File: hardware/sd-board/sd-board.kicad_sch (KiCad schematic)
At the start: 9 parts, among them J1 TF-01A push-push, J2 FFC 6P 0.5mm, U1 74LVC1G04

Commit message: feat(hardware): SD board v4, the user's plan: a 28.8 x 44.5 mm board right of the battery by its plug (the battery stays), the card through the bottom wall flush with the outside at 86 mm from the left wall, the cover's pole in a half-round seat, the FFC from the jacks' gap down to the top; FFC order 3V3 CS MOSI GND CLK MISO (the card's contacts' order, nothing crosses); all sizes measured (MEASUREMENTS.md); DRC 0, nets 0 differ
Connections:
- net 3V3: now also J2.1 (Pin_1); no longer J2.5 (Pin_5)
- net CLK: now also J2.5 (Pin_5); no longer J2.2 (Pin_2)
- net LCD_CS: now also J2.2 (Pin_2); no longer J2.6 (Pin_6)
- net MISO: now also J2.6 (Pin_6); no longer J2.3 (Pin_3)
- net MOSI: now also J2.3 (Pin_3); no longer J2.1 (Pin_1)
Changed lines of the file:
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@@
 (label "3V3" (at 76.2 128.27 270) (effects (font (size 1.27 1.27)) (justify left bottom)))
 (symbol (lib_id "Connector_Generic_MountingPin:Conn_01x06_MountingPin") (at 231.14 88.9 0) (unit 1) (exclude_from_sim no) (in_bom yes) (on_board yes) (dnp no) (property "Reference" "J2" (at 231.14 74.9 0) (effects (font (size 1.27 1.27)))) (property "Value" "FFC 6P 0.5mm" (at 231.14 102.9 0) (effects (font (size 1.27 1.27)))) (property "Footprint" "sdboard:FPC-SMD_6P-P0.50_XUNPU_FPC-05F-6PH20" (at 231.14 88.9 0) (effects (font (size 1.27 1.27)) (hide yes))) (property "Datasheet" "" (at 231.14 88.9 0) (effects (font (size 1.27 1.27)) (hide yes))) (property "LCSC" "C2856796" (at 231.14 88.9 0) (effects (font (size 1.27 1.27)) (hide yes))) (pin "1") (pin "2") (pin "3") (pin "4") (pin "5") (pin "6") (pin "MP") (instances (project "sd-board" (path "/766c70bd-1acb-59f5-b703-96c0315a8041" (reference "J2") (unit 1)))))
-(label "MOSI" (at 226.06 83.82 180) (effects (font (size 1.27 1.27)) (justify right bottom)))
-(label "CLK" (at 226.06 86.36 180) (effects (font (size 1.27 1.27)) (justify right bottom)))
-(label "MISO" (at 226.06 88.9 180) (effects (font (size 1.27 1.27)) (justify right bottom)))
+(label "3V3" (at 226.06 83.82 180) (effects (font (size 1.27 1.27)) (justify right bottom)))
+(label "LCD_CS" (at 226.06 86.36 180) (effects (font (size 1.27 1.27)) (justify right bottom)))
+(label "MOSI" (at 226.06 88.9 180) (effects (font (size 1.27 1.27)) (justify right bottom)))
 (label "GND" (at 226.06 91.44 180) (effects (font (size 1.27 1.27)) (justify right bottom)))
-(label "3V3" (at 226.06 93.98 180) (effects (font (size 1.27 1.27)) (justify right bottom)))
-(label "LCD_CS" (at 226.06 96.52 180) (effects (font (size 1.27 1.27)) (justify right bottom)))
+(label "CLK" (at 226.06 93.98 180) (effects (font (size 1.27 1.27)) (justify right bottom)))
+(label "MISO" (at 226.06 96.52 180) (effects (font (size 1.27 1.27)) (justify right bottom)))
 (label "GND" (at 231.14 101.6 270) (effects (font (size 1.27 1.27)) (justify left bottom)))
 (symbol (lib_id "power:PWR_FLAG") (at 40.64 149.86 0) (unit 1) (exclude_from_sim no) (in_bom no) (on_board no) (dnp no) (property "Reference" "#FLG01" (at 40.64 135.86 0) (effects (font (size 1.27 1.27)) (hide yes))) (property "Value" "PWR_FLAG" (at 40.64 163.86 0) (effects (font (size 1.27 1.27)) (hide yes))) (property "Footprint" "" (at 40.64 149.86 0) (effects (font (size 1.27 1.27)) (hide yes))) (property "Datasheet" "" (at 40.64 149.86 0) (effects (font (size 1.27 1.27)) (hide yes))) (property "LCSC" "" (at 40.64 149.86 0) (effects (font (size 1.27 1.27)) (hide yes))) (pin "1") (instances (project "sd-board" (path "/766c70bd-1acb-59f5-b703-96c0315a8041" (reference "#FLG01") (unit 1)))))

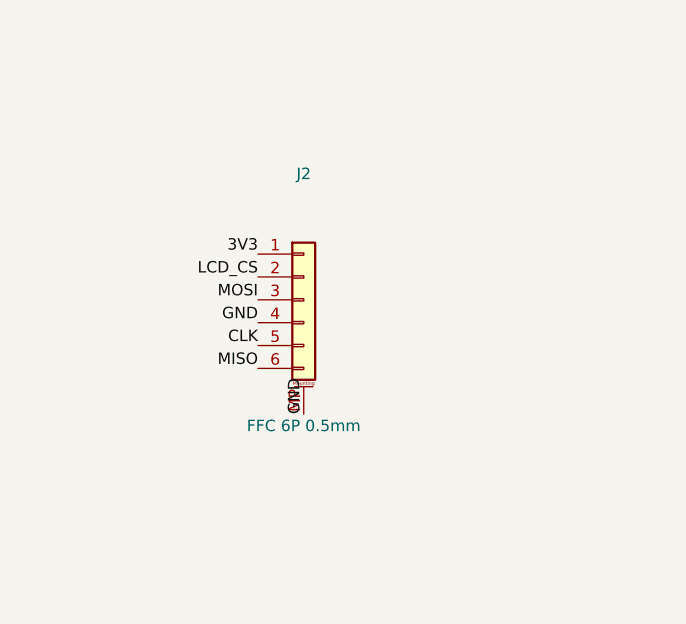
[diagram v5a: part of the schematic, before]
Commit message: feat(hardware): SD board v5, the board is also the splitter (the user): two 10-pin 0.5 mm sockets (HCTL HC-FPC-05-09-10RLTAG, C5213750: JLCPCB stock and SMT assembly, contacts on both sides, 1 mm tall), J3 for the LCD's own cable against the jacks, J2 for a cable from J12 below it, all 10 lines through; a column up the right of the speaker plug to a head under the jacks; the tray stays under the lower part. The J12 pin order is a PROVISIONAL guess (LCD_PINS): not to be ordered before the pin map; DRC 0, nets 0 differ
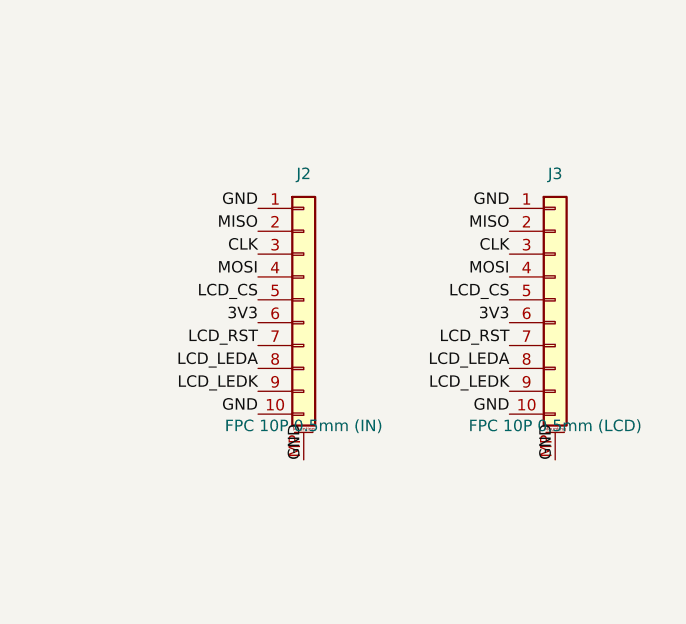
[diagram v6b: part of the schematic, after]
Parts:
- added J3: FPC 10P 0.5mm (LCD), sdboard:FPC-SMD_10P-P0.50_HC-FPC-05-09-10RLTAG, symbol Connector_Generic_MountingPin:Conn_01x10_MountingPin
- J2: value FFC 6P 0.5mm -> FPC 10P 0.5mm (IN); footprint sdboard:FPC-SMD_6P-P0.50_XUNPU_FPC-05F-6PH20 -> sdboard:FPC-SMD_10P-P0.50_HC-FPC-05-09-10RLTAG; symbol Connector_Generic_MountingPin:Conn_01x06_MountingPin -> Connector_Generic_MountingPin:Conn_01x10_MountingPin; LCSC C2856796 -> C5213750
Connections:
- net 3V3: now also J2.6 (Pin_6), J3.6 (Pin_6); no longer J2.1 (Pin_1)
- net CLK: now also J2.3 (Pin_3), J3.3 (Pin_3); no longer J2.5 (Pin_5)
- net GND: now also J2.1 (Pin_1), J2.10 (Pin_10), J3.1 (Pin_1), J3.10 (Pin_10), J3.MP (MountPin); no longer J2.4 (Pin_4)
- net LCD_CS: now also J2.5 (Pin_5), J3.5 (Pin_5); no longer J2.2 (Pin_2)
- net MISO: now also J2.2 (Pin_2), J3.2 (Pin_2); no longer J2.6 (Pin_6)
- net MOSI: now also J2.4 (Pin_4), J3.4 (Pin_4); no longer J2.3 (Pin_3)
- new net LCD_LEDA: J2.8 (Pin_8), J3.8 (Pin_8)
- new net LCD_LEDK: J2.9 (Pin_9), J3.9 (Pin_9)
- new net LCD_RST: J2.7 (Pin_7), J3.7 (Pin_7)
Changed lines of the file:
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@@
 (label "GND" (at 76.2 120.65 90) (effects (font (size 1.27 1.27)) (justify left bottom)))
 (label "3V3" (at 76.2 128.27 270) (effects (font (size 1.27 1.27)) (justify left bottom)))
-(symbol (lib_id "Connector_Generic_MountingPin:Conn_01x06_MountingPin") (at 231.14 88.9 0) (unit 1) (exclude_from_sim no) (in_bom yes) (on_board yes) (dnp no) (property "Reference" "J2" (at 231.14 74.9 0) (effects (font (size 1.27 1.27)))) (property "Value" "FFC 6P 0.5mm" (at 231.14 102.9 0) (effects (font (size 1.27 1.27)))) (property "Footprint" "sdboard:FPC-SMD_6P-P0.50_XUNPU_FPC-05F-6PH20" (at 231.14 88.9 0) (effects (font (size 1.27 1.27)) (hide yes))) (property "Datasheet" "" (at 231.14 88.9 0) (effects (font (size 1.27 1.27)) (hide yes))) (property "LCSC" "C2856796" (at 231.14 88.9 0) (effects (font (size 1.27 1.27)) (hide yes))) (pin "1") (pin "2") (pin "3") (pin "4") (pin "5") (pin "6") (pin "MP") (instances (project "sd-board" (path "/766c70bd-1acb-59f5-b703-96c0315a8041" (reference "J2") (unit 1)))))
-(label "3V3" (at 226.06 83.82 180) (effects (font (size 1.27 1.27)) (justify right bottom)))
-(label "LCD_CS" (at 226.06 86.36 180) (effects (font (size 1.27 1.27)) (justify right bottom)))
-(label "MOSI" (at 226.06 88.9 180) (effects (font (size 1.27 1.27)) (justify right bottom)))
-(label "GND" (at 226.06 91.44 180) (effects (font (size 1.27 1.27)) (justify right bottom)))
-(label "CLK" (at 226.06 93.98 180) (effects (font (size 1.27 1.27)) (justify right bottom)))
-(label "MISO" (at 226.06 96.52 180) (effects (font (size 1.27 1.27)) (justify right bottom)))
-(label "GND" (at 231.14 101.6 270) (effects (font (size 1.27 1.27)) (justify left bottom)))
+(symbol (lib_id "Connector_Generic_MountingPin:Conn_01x10_MountingPin") (at 231.14 88.9 0) (unit 1) (exclude_from_sim no) (in_bom yes) (on_board yes) (dnp no) (property "Reference" "J2" (at 231.14 74.9 0) (effects (font (size 1.27 1.27)))) (property "Value" "FPC 10P 0.5mm (IN)" (at 231.14 102.9 0) (effects (font (size 1.27 1.27)))) (property "Footprint" "sdboard:FPC-SMD_10P-P0.50_HC-FPC-05-09-10RLTAG" (at 231.14 88.9 0) (effects (font (size 1.27 1.27)) (hide yes))) (property "Datasheet" "" (at 231.14 88.9 0) (effects (font (size 1.27 1.27)) (hide yes))) (property "LCSC" "C5213750" (at 231.14 88.9 0) (effects (font (size 1.27 1.27)) (hide yes))) (pin "1") (pin "2") (pin "3") (pin "4") (pin "5") (pin "6") (pin "7") (pin "8") (pin "9") (pin "10") (pin "MP") (instances (project "sd-board" (path "/766c70bd-1acb-59f5-b703-96c0315a8041" (reference "J2") (unit 1)))))
+(label "GND" (at 226.06 78.74 180) (effects (font (size 1.27 1.27)) (justify right bottom)))
+(label "MISO" (at 226.06 81.28 180) (effects (font (size 1.27 1.27)) (justify right bottom)))
+(label "CLK" (at 226.06 83.82 180) (effects (font (size 1.27 1.27)) (justify right bottom)))
+(label "MOSI" (at 226.06 86.36 180) (effects (font (size 1.27 1.27)) (justify right bottom)))
+(label "LCD_CS" (at 226.06 88.9 180) (effects (font (size 1.27 1.27)) (justify right bottom)))
+(label "3V3" (at 226.06 91.44 180) (effects (font (size 1.27 1.27)) (justify right bottom)))
+(label "LCD_RST" (at 226.06 93.98 180) (effects (font (size 1.27 1.27)) (justify right bottom)))
+(label "LCD_LEDA" (at 226.06 96.52 180) (effects (font (size 1.27 1.27)) (justify right bottom)))
+(label "LCD_LEDK" (at 226.06 99.06 180) (effects (font (size 1.27 1.27)) (justify right bottom)))
+(label "GND" (at 226.06 101.6 180) (effects (font (size 1.27 1.27)) (justify right bottom)))
+(label "GND" (at 231.14 106.68 270) (effects (font (size 1.27 1.27)) (justify left bottom)))
+(symbol (lib_id "Connector_Generic_MountingPin:Conn_01x10_MountingPin") (at 259.08 88.9 0) (unit 1) (exclude_from_sim no) (in_bom yes) (on_board yes) (dnp no) (property "Reference" "J3" (at 259.08 74.9 0) (effects (font (size 1.27 1.27)))) (property "Value" "FPC 10P 0.5mm (LCD)" (at 259.08 102.9 0) (effects (font (size 1.27 1.27)))) (property "Footprint" "sdboard:FPC-SMD_10P-P0.50_HC-FPC-05-09-10RLTAG" (at 259.08 88.9 0) (effects (font (size 1.27 1.27)) (hide yes))) (property "Datasheet" "" (at 259.08 88.9 0) (effects (font (size 1.27 1.27)) (hide yes))) (property "LCSC" "C5213750" (at 259.08 88.9 0) (effects (font (size 1.27 1.27)) (hide yes))) (pin "1") (pin "2") (pin "3") (pin "4") (pin "5") (pin "6") (pin "7") (pin "8") (pin "9") (pin "10") (pin "MP") (instances (project "sd-board" (path "/766c70bd-1acb-59f5-b703-96c0315a8041" (reference "J3") (unit 1)))))
+(label "GND" (at 254.0 78.74 180) (effects (font (size 1.27 1.27)) (justify right bottom)))
+(label "MISO" (at 254.0 81.28 180) (effects (font (size 1.27 1.27)) (justify right bottom)))
+(label "CLK" (at 254.0 83.82 180) (effects (font (size 1.27 1.27)) (justify right bottom)))
+(label "MOSI" (at 254.0 86.36 180) (effects (font (size 1.27 1.27)) (justify right bottom)))
+(label "LCD_CS" (at 254.0 88.9 180) (effects (font (size 1.27 1.27)) (justify right bottom)))
+(label "3V3" (at 254.0 91.44 180) (effects (font (size 1.27 1.27)) (justify right bottom)))
+(label "LCD_RST" (at 254.0 93.98 180) (effects (font (size 1.27 1.27)) (justify right bottom)))
+(label "LCD_LEDA" (at 254.0 96.52 180) (effects (font (size 1.27 1.27)) (justify right bottom)))
+(label "LCD_LEDK" (at 254.0 99.06 180) (effects (font (size 1.27 1.27)) (justify right bottom)))
+(label "GND" (at 254.0 101.6 180) (effects (font (size 1.27 1.27)) (justify right bottom)))
+(label "GND" (at 259.08 106.68 270) (effects (font (size 1.27 1.27)) (justify left bottom)))
 (symbol (lib_id "power:PWR_FLAG") (at 40.64 149.86 0) (unit 1) (exclude_from_sim no) (in_bom no) (on_board no) (dnp no) (property "Reference" "#FLG01" (at 40.64 135.86 0) (effects (font (size 1.27 1.27)) (hide yes))) (property "Value" "PWR_FLAG" (at 40.64 163.86 0) (effects (font (size 1.27 1.27)) (hide yes))) (property "Footprint" "" (at 40.64 149.86 0) (effects (font (size 1.27 1.27)) (hide yes))) (property "Datasheet" "" (at 40.64 149.86 0) (effects (font (size 1.27 1.27)) (hide yes))) (property "LCSC" "" (at 40.64 149.86 0) (effects (font (size 1.27 1.27)) (hide yes))) (pin "1") (instances (project "sd-board" (path "/766c70bd-1acb-59f5-b703-96c0315a8041" (reference "#FLG01") (unit 1)))))
 (label "3V3" (at 40.64 149.86 0) (effects (font (size 1.27 1.27)) (justify left bottom)))
